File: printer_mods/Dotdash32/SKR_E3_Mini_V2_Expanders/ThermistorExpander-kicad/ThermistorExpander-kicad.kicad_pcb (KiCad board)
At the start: 2 copper layers, 20.5 x 14.2 mm, 8 parts, among them J1 SPI1_breakaway, J2 Conn_01x02, J3 Conn_01x02, J4 Conn_01x02

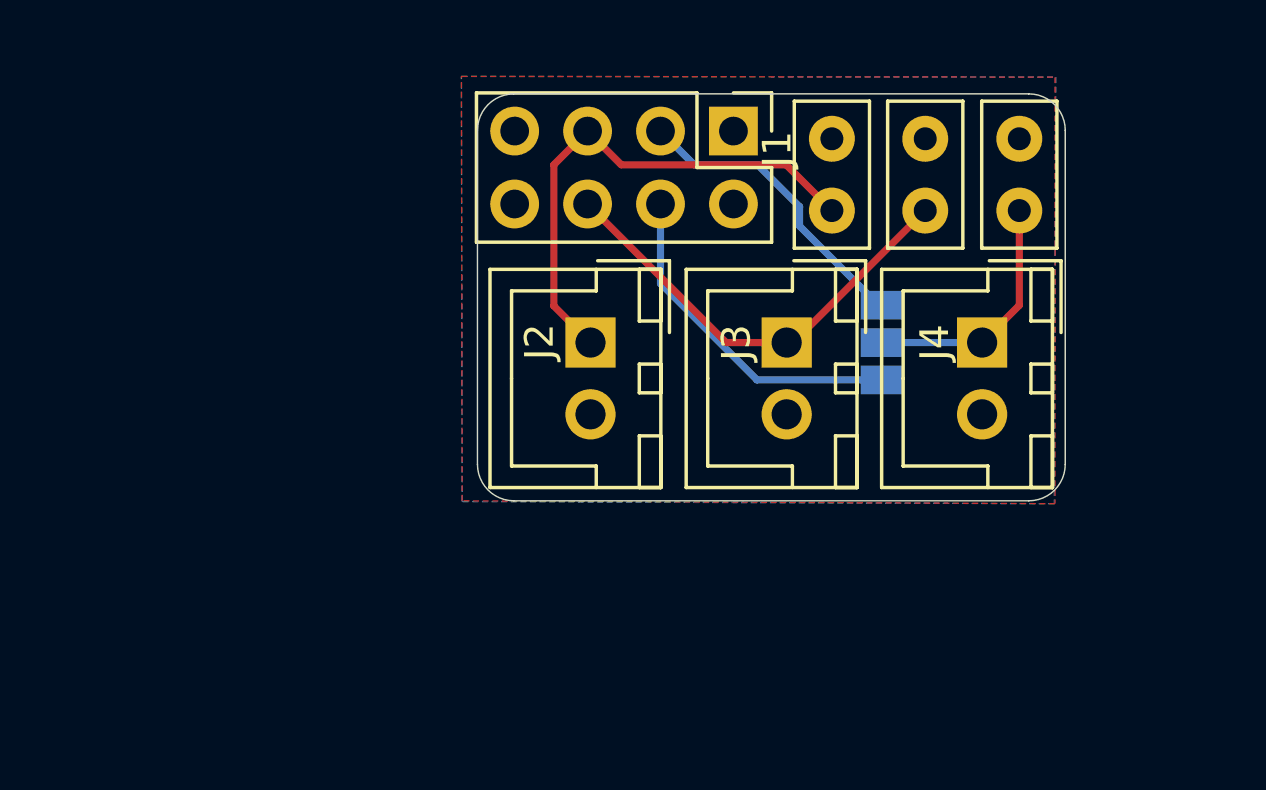
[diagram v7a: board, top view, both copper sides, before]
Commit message: test: LCSC larger THT capacitor
it's sooo bigg though...
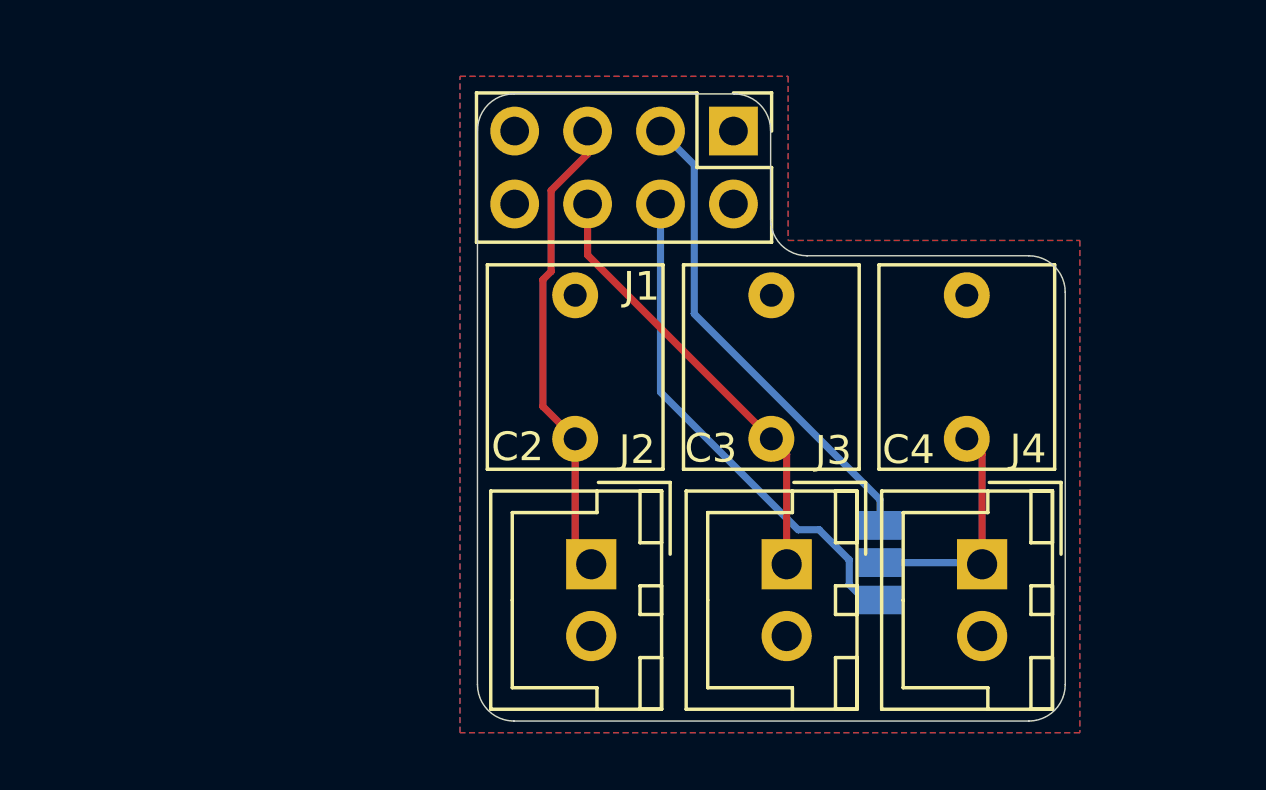
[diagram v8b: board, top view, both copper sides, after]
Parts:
- removed C1: 10uF, Capacitors_THT:C_Disc_D5.0mm_W2.5mm_P2.50mm
- added C2: 10uF, Capacitors_THT:C_Rect_L7.0mm_W6.0mm_P5.00mm, F.Cu at (122.8, 85.6)
- C3: renamed from C2; footprint Capacitors_THT:C_Disc_D5.0mm_W2.5mm_P2.50mm -> Capacitors_THT:C_Rect_L7.0mm_W6.0mm_P5.00mm
- C4: renamed from C3; footprint Capacitors_THT:C_Disc_D5.0mm_W2.5mm_P2.50mm -> Capacitors_THT:C_Rect_L7.0mm_W6.0mm_P5.00mm
- J1: value SPI1_breakaway -> SPI_Header
- J2, J3, J4: value Conn_01x02 -> JST-XH2
- JP1: value Jumper_3_Open -> V2-3_SEL
- moved C3 9.59 mm to (129.6, 85.6)
- moved C4 8.16 mm to (136.4, 85.6)
- moved J2 7.72 mm to (123.3, 90.0)
- moved J3 7.72 mm to (130.1, 90.0)
- moved J4 7.72 mm to (136.9, 90.0)
- moved JP1 7.67 mm to (133.4, 90.0)
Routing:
- net /V2.0: track 10.6 -> 16.9 mm
- net /V3.0: track 11.9 -> 17.7 mm
- net /TH2: track 18.0 -> 16.4 mm
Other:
- board size 20.5 x 14.2 mm -> 20.5 x 21.8 mm
- board text added: "JLCJLCJLCJLC"
- board text added: "SPI TH Exp V1.0 by Dotdash32 (JDeW)"
- board text removed: "Dotdash32 (JDeW)"
- board text removed: "JLCJLCJLC"
- board text removed: "SPI TH Exp V1.0"
